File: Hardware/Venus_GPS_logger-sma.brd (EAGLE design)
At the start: 31.8 x 19.1 mm, 22 parts, among them U1 VENUS634SMD, U2 33nH, U3 V_REG_LDOSMD, U4 SPI_FLASH-X25XXSMD1

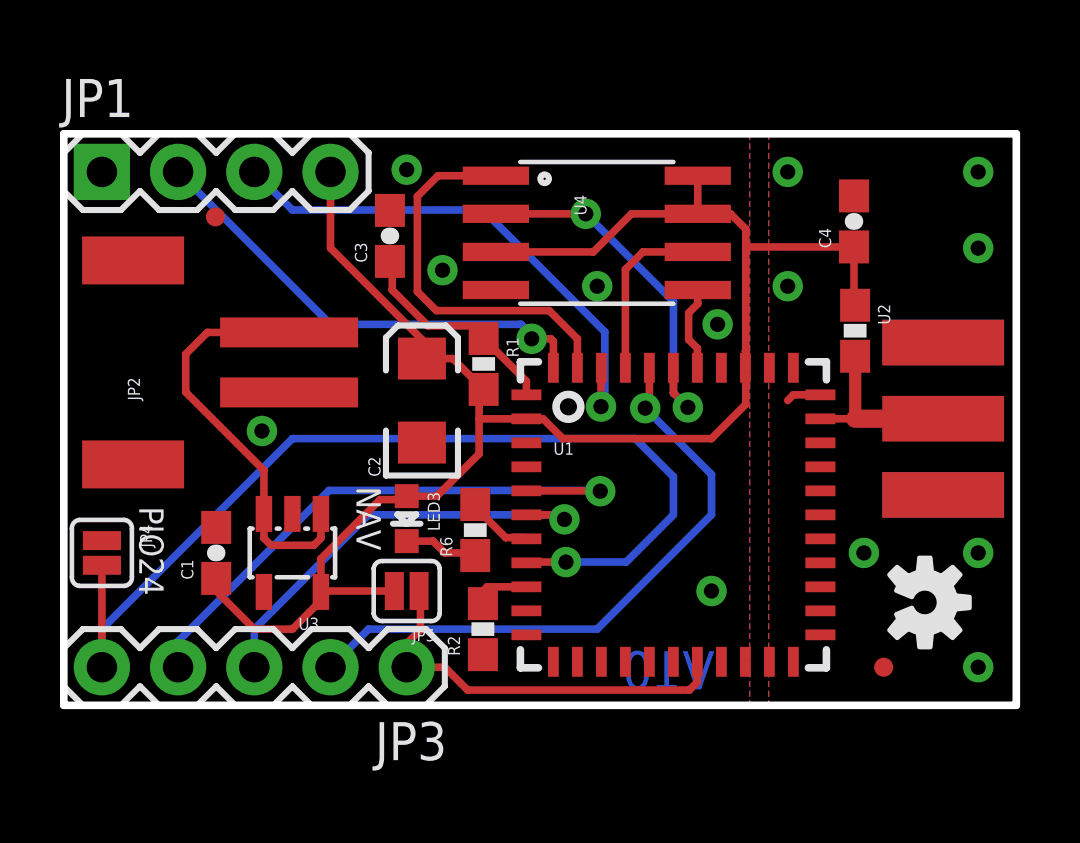
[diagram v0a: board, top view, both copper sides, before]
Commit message: Updated LED, fixed questionable trace routes
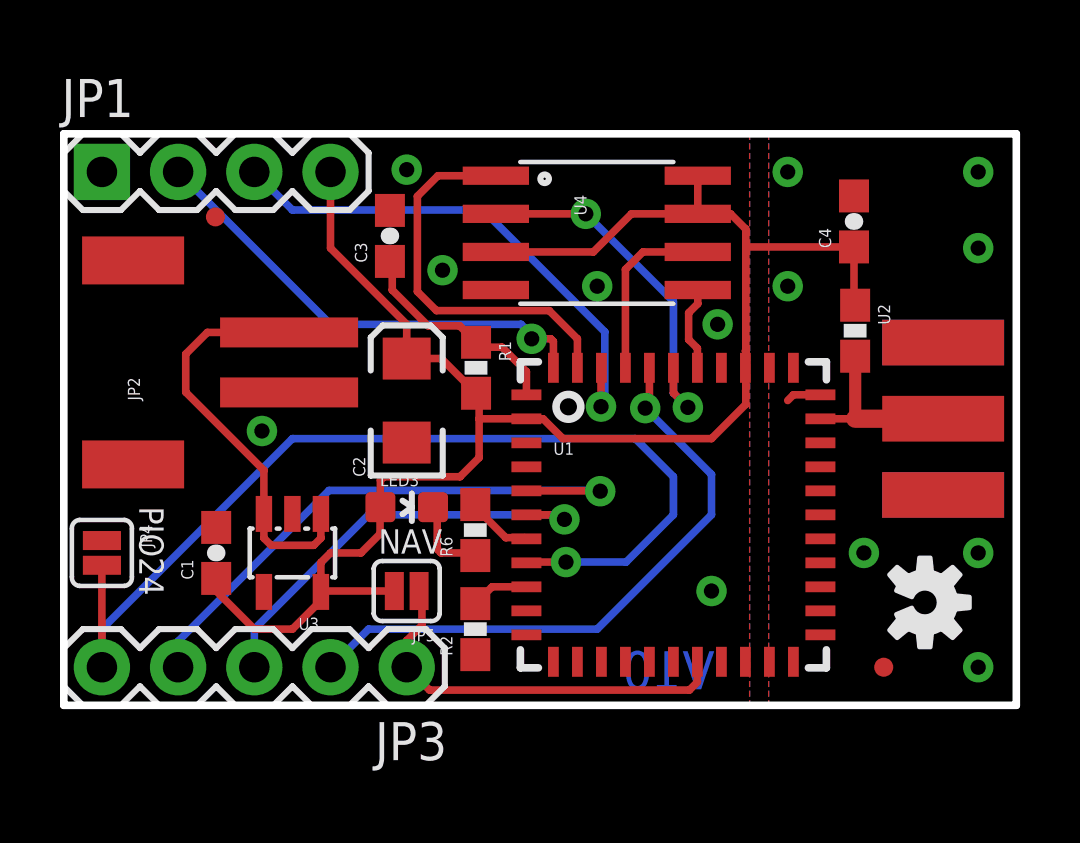
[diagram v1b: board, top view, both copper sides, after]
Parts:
- added FRAME1: FRAME-LETTER, SparkFun-Aesthetics:CREATIVE_COMMONS
- LED3: device SparkFun:LED-0603 -> SparkFun-LED:LED-0603
- moved C2 0.51 mm to (11.4, 10.2)
- moved LED3 0.38 mm to (11.4, 6.60), turned to 270 degrees
- moved R1 0.28 mm to (13.7, 11.3)
- moved R2 0.25 mm to (13.7, 2.54)
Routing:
- net 3.3V: track 59.3 -> 60.8 mm

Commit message: Moved Jumper
Moved jumper to the bttm copper, and changed silk on the jpm to "low
power".
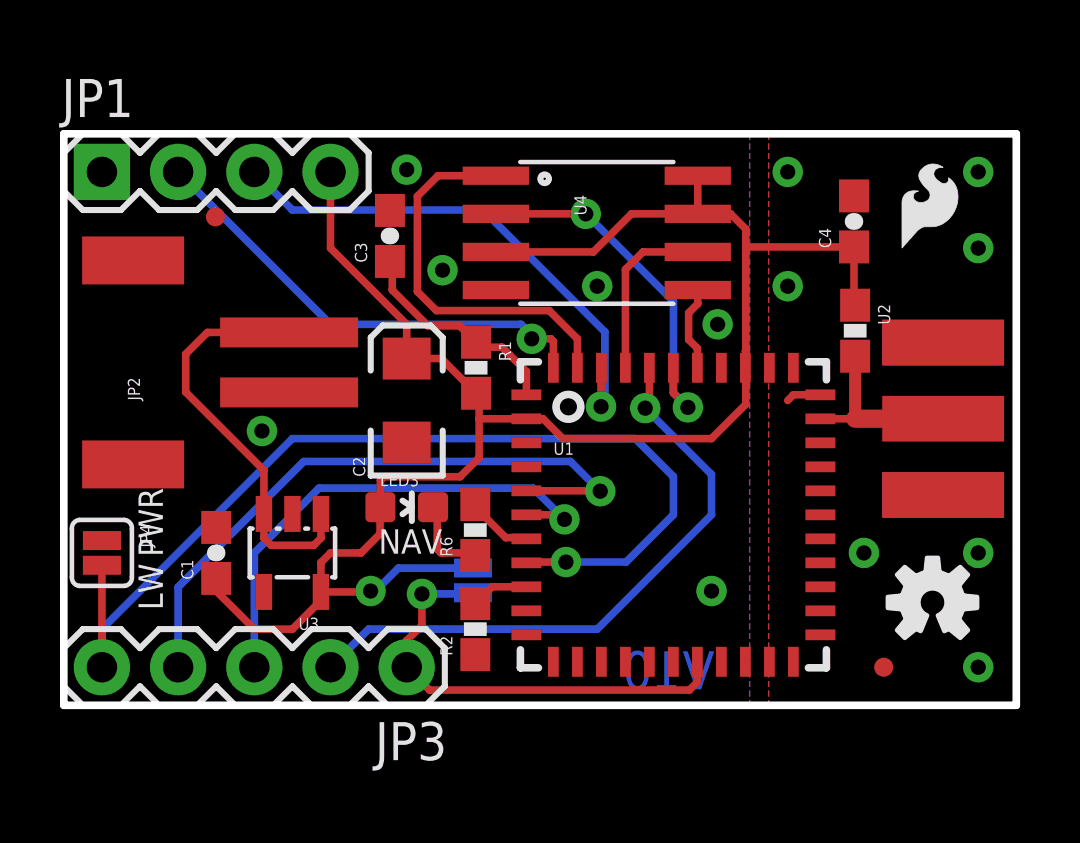
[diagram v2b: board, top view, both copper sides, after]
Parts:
- added U$3: (no value), SparkFun-Aesthetics:SFE-NEW-WEBLOGO
- moved U$1 24.7 mm to (27.9, 15.2), flipped to the top, turned to 0 degrees
- moved JP5 2.24 mm to (13.6, 4.17), flipped to the bottom, turned to 90 degrees
- moved U$2 0.25 mm to (29.0, 3.43), turned to 0 degrees
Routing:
- net 3.3V: track 60.8 -> 63.7 mm, vias 0 -> 1
- net GPIO1: track 14.6 -> 17.0 mm
- net GPIO2: track 19.5 -> 21.4 mm
- net VBAT: track 13.6 -> 15.2 mm, vias 0 -> 1
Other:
- board text added: "LW"
- board text added: "PWR"
- board text added: "Venus GPS Logger"
- board text removed: "PIO24"
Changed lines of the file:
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@@
 <?xml version="1.0" encoding="utf-8"?>
 <!DOCTYPE eagle SYSTEM "eagle.dtd">
-<eagle version="6.5.0">
+<eagle version="6.4">
 <drawing>
 <settings>
@@
 <layer number="27" name="tValues" color="7" fill="1" visible="no" active="yes"/>
 <layer number="28" name="bValues" color="7" fill="1" visible="no" active="yes"/>
-<layer number="29" name="tStop" color="7" fill="3" visible="yes" active="yes"/>
+<layer number="29" name="tStop" color="7" fill="3" visible="no" active="yes"/>
 <layer number="30" name="bStop" color="7" fill="6" visible="no" active="yes"/>
 <layer number="31" name="tCream" color="7" fill="4" visible="no" active="yes"/>
@@
 <wire x1="31.75" y1="19.05" x2="0" y2="19.05" width="0.254" layer="20"/>
 <wire x1="0" y1="19.05" x2="0" y2="0" width="0.254" layer="20"/>
-<text x="2.5146" y="6.6294" size="0.8128" layer="21" font="vector" ratio="15" rot="SR270">PIO24</text>
 <text x="10.4902" y="5.0546" size="0.8128" layer="21" font="vector" ratio="15" rot="SR0">NAV</text>
 <text x="9.271" y="16.129" size="0.8128" layer="22" font="vector" ratio="15" rot="SMR270">3.3V</text>
@@
 <text x="1.778" y="4.191" size="0.8128" layer="22" font="vector" ratio="15" rot="SMR270">24</text>
 <text x="21.6916" y="0.5334" size="1.27" layer="16" font="vector" ratio="18" rot="MR0">V10</text>
+<text x="27.94" y="6.35" size="1.778" layer="22" font="vector" ratio="15" rot="MR0">Venus GPS Logger</text>
+<text x="3.302" y="4.953" size="0.8128" layer="21" font="vector" ratio="15" rot="R90">PWR</text>
+<text x="3.302" y="3.175" size="0.8128" layer="21" font="vector" ratio="15" rot="R90">LW</text>
 </plain>
 <attributes>
@@
 <element name="JP1" library="SparkFun-Connectors" package="1X04" value="UART" x="1.27" y="17.78"/>
 <element name="JP3" library="SparkFun-Connectors" package="1X05" value="General" x="11.43" y="1.27" rot="R180"/>
-<element name="U$1" library="SparkFun" package="SFE-LOGO-FLAME" value="LOGO-SFESK" x="3.81" y="10.16" rot="MR270"/>
+<element name="U$1" library="SparkFun" package="SFE-LOGO-FLAME" value="LOGO-SFESK" x="27.94" y="15.24"/>
 <element name="U2" library="SparkFun-Resistors" package="0603-RES" value="33nH" x="26.3779" y="12.4867" rot="R270">
 <attribute name="PROD_ID" value="NDUC-07874" x="26.3779" y="12.4867" size="1.778" layer="27" rot="R270" display="off"/>
@@
 <element name="U3" library="SparkFun" package="SOT23-5" value="V_REG_LDOSMD" x="7.62" y="5.08" rot="R180"/>
 <element name="JP4" library="SparkFun-Passives" package="SJ_2S" value="Low Power Mode" x="1.27" y="5.08" rot="R270"/>
-<element name="JP5" library="SparkFun-Passives" package="SJ_2S" value="VBAT Select" x="11.43" y="3.81" rot="R180"/>
+<element name="JP5" library="SparkFun-Passives" package="SJ_2S" value="VBAT Select" x="13.6398" y="4.1656" rot="MR90"/>
 <element name="JP6" library="abes" package="FIDUCIAL-1X2.5" value="FIDUCIAL1X2.5" x="5.0546" y="16.2814"/>
 <element name="JP7" library="abes" package="FIDUCIAL-1X2.5" value="FIDUCIAL1X2.5" x="27.3304" y="1.27"/>
-<element name="U$2" library="SparkFun-Aesthetics" package="OSHW-LOGO-S" value="" x="28.702" y="3.429" rot="R270"/>
+<element name="U$2" library="SparkFun-Aesthetics" package="OSHW-LOGO-S" value="" x="28.956" y="3.429"/>
 <element name="FRAME1" library="SparkFun-Aesthetics" package="CREATIVE_COMMONS" value="FRAME-LETTER" x="-88.66845625" y="0"/>
+<element name="U$3" library="SparkFun-Aesthetics" package="SFE-NEW-WEBLOGO" value="" x="25.4" y="8.89" rot="MR0"/>
 </elements>
 <signals>
@@
 <wire x1="7.62" y1="2.54" x2="8.57" y2="3.49" width="0.254" layer="1"/>
 <wire x1="6.35" y1="2.54" x2="7.62" y2="2.54" width="0.254" layer="1"/>
-<wire x1="8.57" y1="3.7799" x2="8.6001" y2="3.81" width="0.254" layer="1"/>
-<wire x1="8.6001" y1="3.81" x2="11.0181" y2="3.81" width="0.254" layer="1"/>
 <wire x1="13.843" y1="10.16" x2="13.843" y2="10.453" width="0.254" layer="1"/>
 <wire x1="15.42" y1="9.55" x2="13.843" y2="9.55" width="0.254" layer="1"/>
@@
 <wire x1="13.7414" y1="10.4022" x2="13.7414" y2="10.3886" width="0.254" layer="1"/>
 <wire x1="13.7414" y1="10.3886" x2="13.9065" y2="10.2235" width="0.254" layer="1"/>
+<via x="10.2257" y="3.81" extent="1-16" drill="0.508"/>
+<wire x1="8.57" y1="3.7799" x2="10.1956" y2="3.7799" width="0.254" layer="1"/>
+<wire x1="10.1956" y1="3.7799" x2="10.2257" y2="3.81" width="0.254" layer="1"/>
+<wire x1="10.2257" y1="3.81" x2="10.3886" y2="3.81" width="0.254" layer="16"/>
+<wire x1="10.3886" y1="3.81" x2="11.1506" y2="4.572" width="0.254" layer="16"/>
+<wire x1="11.1506" y1="4.572" x2="13.6343" y2="4.572" width="0.254" layer="16"/>
+<wire x1="13.6343" y1="4.572" x2="13.6398" y2="4.5775" width="0.254" layer="16"/>
 </signal>
 <signal name="N$1">
@@
 <contactref element="U1" pad="6"/>
 <contactref element="JP3" pad="3"/>
-<wire x1="6.35" y1="1.27" x2="6.35" y2="2.54" width="0.254" layer="16"/>
-<wire x1="6.35" y1="2.54" x2="10.16" y2="6.35" width="0.254" layer="16"/>
 <via x="16.6878" y="6.1976" extent="1-16" drill="0.508"/>
 <wire x1="15.42" y1="6.35" x2="16.5354" y2="6.35" width="0.254" layer="1"/>
 <wire x1="16.5354" y1="6.35" x2="16.6878" y2="6.1976" width="0.254" layer="1"/>
-<wire x1="10.16" y1="6.35" x2="16.5354" y2="6.35" width="0.254" layer="16"/>
 <wire x1="16.5354" y1="6.35" x2="16.6878" y2="6.1976" width="0.254" layer="16"/>
+<wire x1="6.35" y1="1.27" x2="6.35" y2="5.08" width="0.254" layer="16"/>
+<wire x1="6.35" y1="5.08" x2="8.509" y2="7.239" width="0.254" layer="16"/>
+<wire x1="8.509" y1="7.239" x2="15.6464" y2="7.239" width="0.254" layer="16"/>
+<wire x1="15.6464" y1="7.239" x2="16.6878" y2="6.1976" width="0.254" layer="16"/>
 </signal>
 <signal name="GPIO2">
@@
 <wire x1="17.869" y1="7.15" x2="15.42" y2="7.15" width="0.254" layer="1"/>
 <wire x1="17.8816" y1="7.1374" x2="17.869" y2="7.15" width="0.254" layer="1"/>
-<wire x1="3.81" y1="1.27" x2="3.81" y2="2.1336" width="0.254" layer="16"/>
 <wire x1="17.8816" y1="7.1374" x2="17.8562" y2="7.112" width="0.254" layer="16"/>
-<wire x1="3.81" y1="2.1336" x2="8.8392" y2="7.1628" width="0.254" layer="16"/>
-<wire x1="8.8392" y1="7.1628" x2="17.8562" y2="7.1628" width="0.254" layer="16"/>
 <wire x1="17.8562" y1="7.1628" x2="17.8816" y2="7.1374" width="0.254" layer="16"/>
 <via x="17.8816" y="7.1374" extent="1-16" drill="0.508"/>
+<wire x1="3.81" y1="1.27" x2="3.81" y2="3.937" width="0.254" layer="16"/>
+<wire x1="3.81" y1="3.937" x2="8.001" y2="8.128" width="0.254" layer="16"/>
+<wire x1="8.001" y1="8.128" x2="16.891" y2="8.128" width="0.254" layer="16"/>
+<wire x1="16.891" y1="8.128" x2="17.8816" y2="7.1374" width="0.254" layer="16"/>
 </signal>
 <signal name="GPIO24">
@@
 <wire x1="21.12" y1="0.7746" x2="21.12" y2="1.45" width="0.254" layer="1"/>
 <wire x1="20.8534" y1="0.508" x2="21.12" y2="0.7746" width="0.254" layer="1"/>
-<wire x1="11.8872" y1="3.7647" x2="11.8419" y2="3.81" width="0.254" layer="1"/>
 <wire x1="12.192" y1="0.508" x2="11.43" y2="1.27" width="0.254" layer="1"/>
 <wire x1="11.43" y1="1.27" x2="11.43" y2="2.159" width="0.254" layer="1"/>
 <wire x1="11.43" y1="2.159" x2="11.938" y2="2.667" width="0.254" layer="1"/>
 <wire x1="11.938" y1="2.667" x2="11.938" y2="3.7139" width="0.254" layer="1"/>
-<wire x1="11.938" y1="3.7139" x2="11.8419" y2="3.81" width="0.254" layer="1"/>
+<via x="11.938" y="3.7139" extent="1-16" drill="0.508"/>
+<wire x1="11.938" y1="3.7139" x2="13.6" y2="3.7139" width="0.254" layer="16"/>
+<wire x1="13.6" y1="3.7139" x2="13.6398" y2="3.7537" width="0.254" layer="16"/>
 </signal>
 </signals>
-<errors>
-</errors>
 </board>
 </drawing>

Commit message: Closed jumper
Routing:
- net N$4: track 0.00 -> 0.69 mm
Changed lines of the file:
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@@
 <setting verticaltext="up"/>
 </settings>
-<grid distance="0.05" unitdist="inch" unit="inch" style="lines" multiple="1" display="yes" altdistance="0.005" altunitdist="inch" altunit="inch"/>
+<grid distance="0.05" unitdist="inch" unit="inch" style="lines" multiple="1" display="yes" altdistance="0.001" altunitdist="inch" altunit="inch"/>
 <layers>
 <layer number="1" name="Top" color="4" fill="1" visible="yes" active="yes"/>
@@
 <layer number="47" name="Measures" color="7" fill="1" visible="no" active="yes"/>
 <layer number="48" name="Document" color="7" fill="1" visible="no" active="yes"/>
-<layer number="49" name="Reference" color="7" fill="1" visible="no" active="yes"/>
+<layer number="49" name="Reference" color="7" fill="1" visible="yes" active="yes"/>
 <layer number="50" name="dxf" color="7" fill="1" visible="no" active="yes"/>
 <layer number="51" name="tDocu" color="6" fill="1" visible="yes" active="yes"/>
@@
 <wire x1="13.6" y1="3.7139" x2="13.6398" y2="3.7537" width="0.254" layer="16"/>
 </signal>
+<signal name="N$2">
+<wire x1="13.589" y1="4.318" x2="13.589" y2="3.937" width="0" layer="19" extent="1-16"/>
+</signal>
+<signal name="N$4">
+<wire x1="13.6398" y1="4.5466" x2="13.6398" y2="3.8608" width="0.2032" layer="16"/>
+</signal>
 </signals>

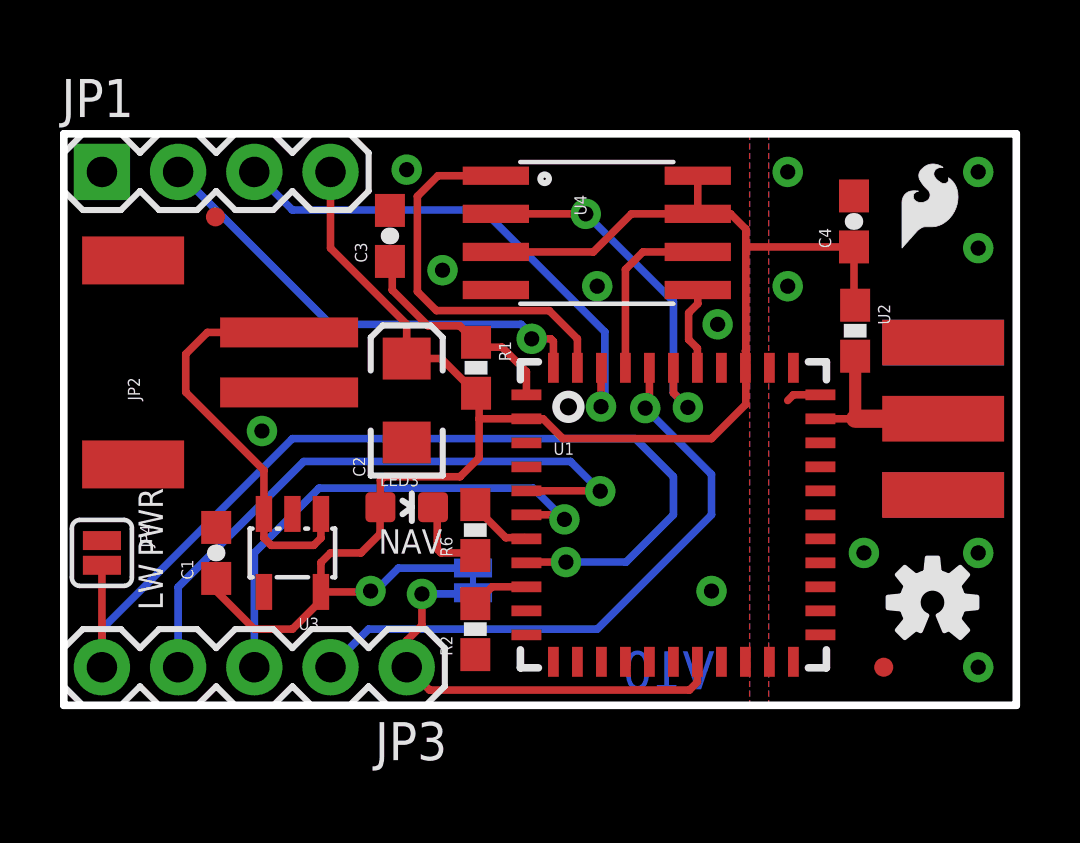
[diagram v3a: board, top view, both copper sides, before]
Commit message: changed fiducials to regular size and repositioned
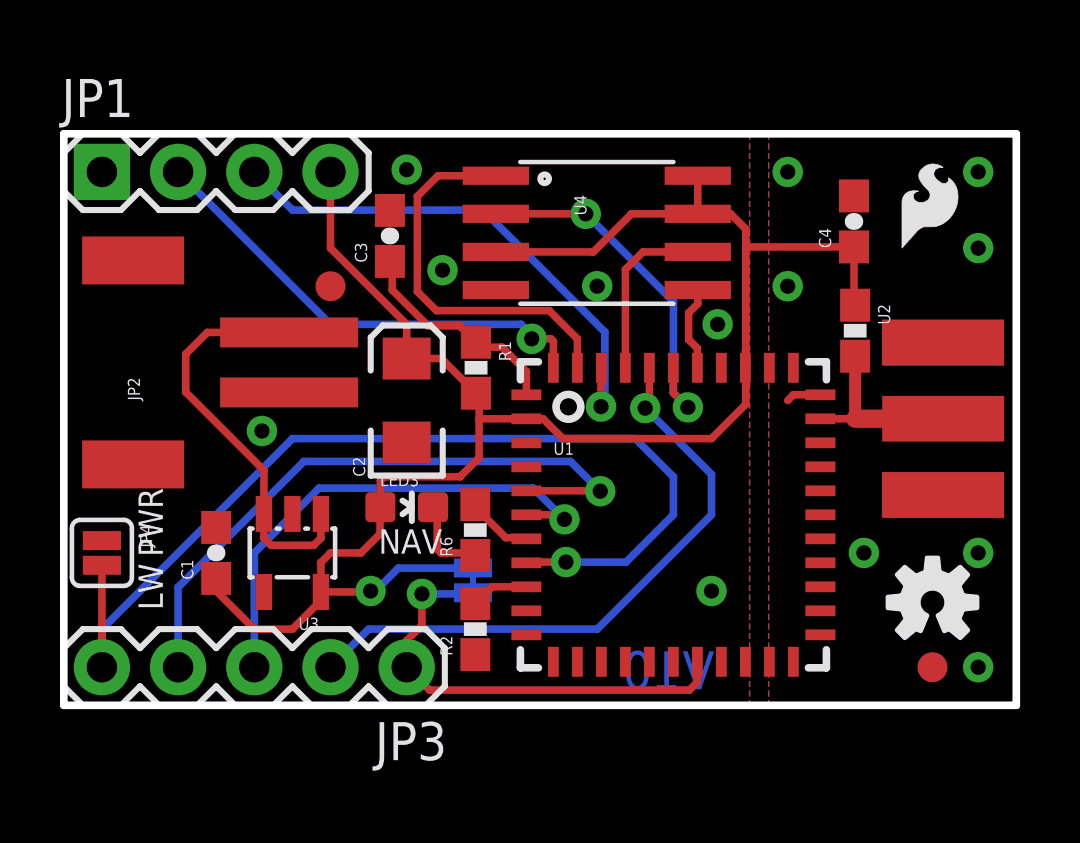
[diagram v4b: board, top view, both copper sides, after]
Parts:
- removed JP6, JP7: FIDUCIAL1X2.5, abes:FIDUCIAL-1X2.5
- added FID1, FID2: FIDUCIAL1X2, SparkFun-Aesthetics:FIDUCIAL-1X2
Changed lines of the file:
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@@
 <?xml version="1.0" encoding="utf-8"?>
 <!DOCTYPE eagle SYSTEM "eagle.dtd">
-<eagle version="6.4">
+<eagle version="6.5.0">
 <drawing>
 <settings>
@@
 <setting verticaltext="up"/>
 </settings>
-<grid distance="0.05" unitdist="inch" unit="inch" style="lines" multiple="1" display="yes" altdistance="0.001" altunitdist="inch" altunit="inch"/>
+<grid distance="0.05" unitdist="inch" unit="inch" style="lines" multiple="1" display="yes" altdistance="0.01" altunitdist="inch" altunit="inch"/>
 <layers>
 <layer number="1" name="Top" color="4" fill="1" visible="yes" active="yes"/>
@@
 <layer number="18" name="Vias" color="2" fill="1" visible="yes" active="yes"/>
 <layer number="19" name="Unrouted" color="6" fill="1" visible="yes" active="yes"/>
-<layer number="20" name="Dimension" color="15" fill="1" visible="yes" active="yes"/>
-<layer number="21" name="tPlace" color="16" fill="1" visible="yes" active="yes"/>
-<layer number="22" name="bPlace" color="14" fill="1" visible="yes" active="yes"/>
+<layer number="20" name="Dimension" color="6" fill="1" visible="yes" active="yes"/>
+<layer number="21" name="tPlace" color="6" fill="1" visible="yes" active="yes"/>
+<layer number="22" name="bPlace" color="6" fill="1" visible="yes" active="yes"/>
 <layer number="23" name="tOrigins" color="15" fill="1" visible="yes" active="yes"/>
 <layer number="24" name="bOrigins" color="15" fill="1" visible="yes" active="yes"/>
@@
 <element name="JP4" library="SparkFun-Passives" package="SJ_2S" value="Low Power Mode" x="1.27" y="5.08" rot="R270"/>
 <element name="JP5" library="SparkFun-Passives" package="SJ_2S" value="VBAT Select" x="13.6398" y="4.1656" rot="MR90"/>
-<element name="JP6" library="abes" package="FIDUCIAL-1X2.5" value="FIDUCIAL1X2.5" x="5.0546" y="16.2814"/>
-<element name="JP7" library="abes" package="FIDUCIAL-1X2.5" value="FIDUCIAL1X2.5" x="27.3304" y="1.27"/>
 <element name="U$2" library="SparkFun-Aesthetics" package="OSHW-LOGO-S" value="" x="28.956" y="3.429"/>
 <element name="FRAME1" library="SparkFun-Aesthetics" package="CREATIVE_COMMONS" value="FRAME-LETTER" x="-88.66845625" y="0"/>
 <element name="U$3" library="SparkFun-Aesthetics" package="SFE-NEW-WEBLOGO" value="" x="25.4" y="8.89" rot="MR0"/>
+<element name="FID1" library="SparkFun-Aesthetics" package="FIDUCIAL-1X2" value="FIDUCIAL1X2" x="28.956" y="1.27"/>
+<element name="FID2" library="SparkFun-Aesthetics" package="FIDUCIAL-1X2" value="FIDUCIAL1X2" x="8.89" y="13.97"/>
 </elements>
 <signals>
@@
 <wire x1="13.6" y1="3.7139" x2="13.6398" y2="3.7537" width="0.254" layer="16"/>
 </signal>
-<signal name="N$2">
-<wire x1="13.589" y1="4.318" x2="13.589" y2="3.937" width="0" layer="19" extent="1-16"/>
-</signal>
 <signal name="N$4">
